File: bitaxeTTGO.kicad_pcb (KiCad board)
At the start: 4 copper layers, 56.5 x 99.8 mm, 133 parts, among them J1 Conn_01x01, J2 Conn_01x01, J3 Conn_01x05, J4 Conn_01x04, J5 TC2030-IDC, J6 Conn_01x08, J7 Conn_01x02, J9 Conn_01x04, Q1 CSD17311Q5, Q2 CSD17311Q5, SW1 GT-TC029B-H025-L1N, SW2 GT-TC029B-H025-L1N, U1 25MHz, U10 DS4432U+, U11 RT9080-33GJ5, U12 ESP32-S3-WROOM-1, U14 BM1366_mode0, U2 TXB0104RGYR, U5 MCP1824T-1802E, U6 MCP1824T-0802E, U7 EMC2101, U8 INA260, U9 TPS40305, Y1 32.768kHz

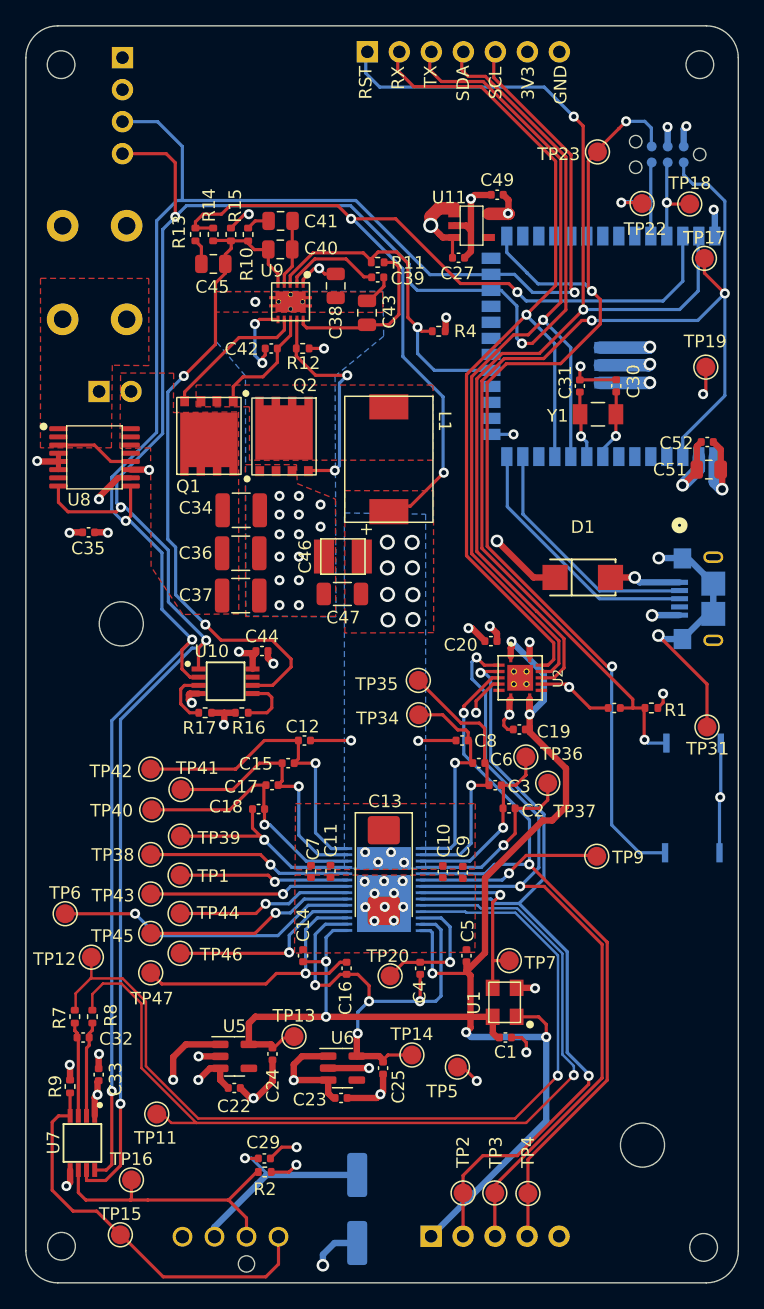
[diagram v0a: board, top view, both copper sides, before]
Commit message: added T-Display-S3 and barrel connector
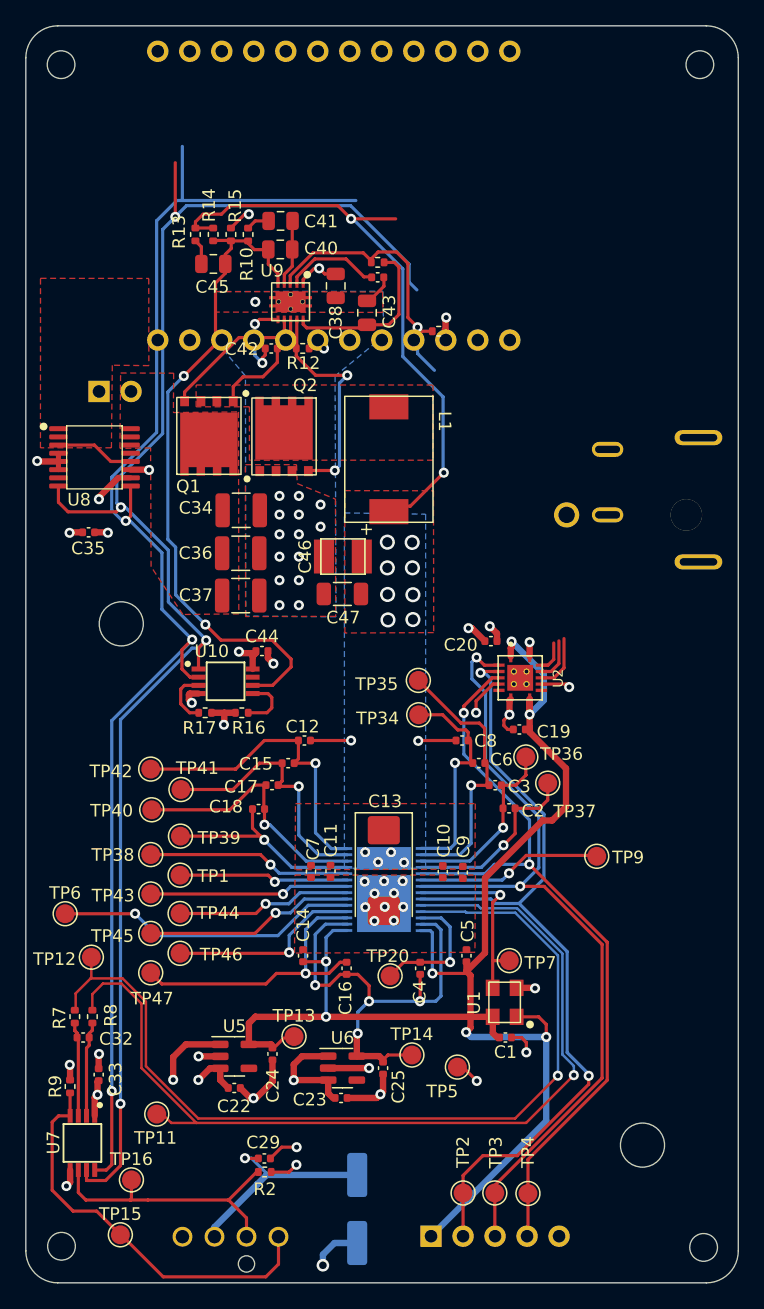
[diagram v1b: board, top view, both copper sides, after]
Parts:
- removed C21, C27, C49: 1uF, Capacitor_SMD:C_0402_1005Metric
- removed C30, C31: 6.8pF, Capacitor_SMD:C_0402_1005Metric
- removed C51: 10uF, Capacitor_SMD:C_0805_2012Metric
- removed C52: 0.1uF, Capacitor_SMD:C_0402_1005Metric
- removed D1: SS310, lcsc:SMA_L4.3-W2.6-LS5.2-RD
- removed J1, J2: Conn_01x01, TPS40305_supply:63862-1
- removed J5: TC2030-IDC, Connector:Tag-Connect_TC2030-IDC-NL_2x03_P1.27mm_Vertical
- removed J6: Conn_01x08, Connector_PinHeader_2.54mm:PinHeader_1x07_P2.54mm_Vertical
- removed J9: Conn_01x04, Connector_PinHeader_2.54mm:PinHeader_1x04_P2.54mm_Vertical
- removed R1: 10k, Resistor_SMD:R_0402_1005Metric
- removed SW1, SW2: GT-TC029B-H025-L1N, bitaxe:SW_CS1213AGF260_CRS
- removed TP17, TP18, TP19, TP22, TP23, TP31: TestPoint, TestPoint:TestPoint_Pad_D1.5mm
- removed U11: RT9080-33GJ5, bitaxe:RT9080-33GJ5
- removed U12: ESP32-S3-WROOM-1, Espressif:ESP32-S3-WROOM-1
- removed USB1: 10118193-0001LF, bitaxe:USB_10118193-0001LF_AMP
- removed Y1: 32.768kHz, bitaxe:SC32S-7PF20PPM
- removed kibuzzard-6392B1E5: G***, kibuzzard-6392B1E5
- added DC1: DC-044K-D025, lcsc:DC-IN-TH_DC-044K-D025, B.Cu at (125.3, 85.1)
- added U3: T-Display-S3, bitaxe:T-Display-S3, B.Cu at (108.9, 61.0)
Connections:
- net /Power/VIN renamed /VIN
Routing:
- net /ESP32/EN: track 89.8 -> 0.00 mm, vias 3 -> 0
- net /ESP32/IO0: track 86.3 -> 0.00 mm, vias 3 -> 0
- net /RST: track 87.8 -> 4.44 mm, vias 2 -> 0
- net /RX: track 75.5 -> 2.48 mm, vias 1 -> 0
- net /TX: track 74.5 -> 3.45 mm, vias 1 -> 0
- net GND: track 126.2 -> 55.5 mm, vias 60 -> 48
- net /SCL: track 159.0 -> 111.5 mm, vias 4 -> 3
- net /SDA: track 169.3 -> 124.1 mm, vias 5 -> 4
- net /VDD: track 83.3 -> 53.6 mm, vias 17 -> 16
- net Net-(U12-GPIO20/U1CTS/ADC2_CH9/CLK_OUT1/USB_D+): track 20.7 -> 0.00 mm
- net Net-(U12-GPIO19/U1RTS/ADC2_CH8/CLK_OUT2/USB_D-): track 19.5 -> 0.00 mm
- net /3V3: track 59.7 -> 42.6 mm, vias 15 -> 9
- net /5V: track 210.0 -> 197.4 mm, vias 7 -> 5
- net /ESP32/P_RX: track 9.97 -> 0.00 mm, vias 1 -> 0
- net /ESP32/P_TX: track 7.79 -> 0.00 mm, vias 1 -> 0
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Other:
- board text added: "BM1366 V2"
- board text removed: "3V3"
- board text removed: "BM1366 V1"
- board text removed: "RX"
- board text removed: "SCL"
- board text removed: "SDA"
- board text removed: "TX"
